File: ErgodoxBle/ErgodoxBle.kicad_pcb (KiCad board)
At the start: 2 copper layers, 179.4 x 159.7 mm, 84 parts, among them K0 KEYSW, K1 KEYSW, K10 KEYSW, K11 KEYSW, K12 KEYSW, K13 KEYSW, K14 KEYSW, K15 KEYSW, K16 KEYSW, K2 KEYSW, K20 KEYSW, K21 KEYSW, K22 KEYSW, K23 KEYSW, K24 KEYSW, K25 KEYSW, K26 KEYSW, K3 KEYSW, K30 KEYSW, K31 KEYSW, K32 KEYSW, K33 KEYSW, K34 KEYSW, K35 KEYSW, K36 KEYSW, K4 KEYSW, K40 KEYSW, K41 KEYSW, K42 KEYSW, K43 KEYSW, K44 KEYSW, K45 KEYSW, K46 KEYSW, K5 KEYSW, K54 KEYSW, K55 KEYSW, K56 KEYSW, K6 KEYSW, SW1 SW_PUSH, SW2 SW_PUSH

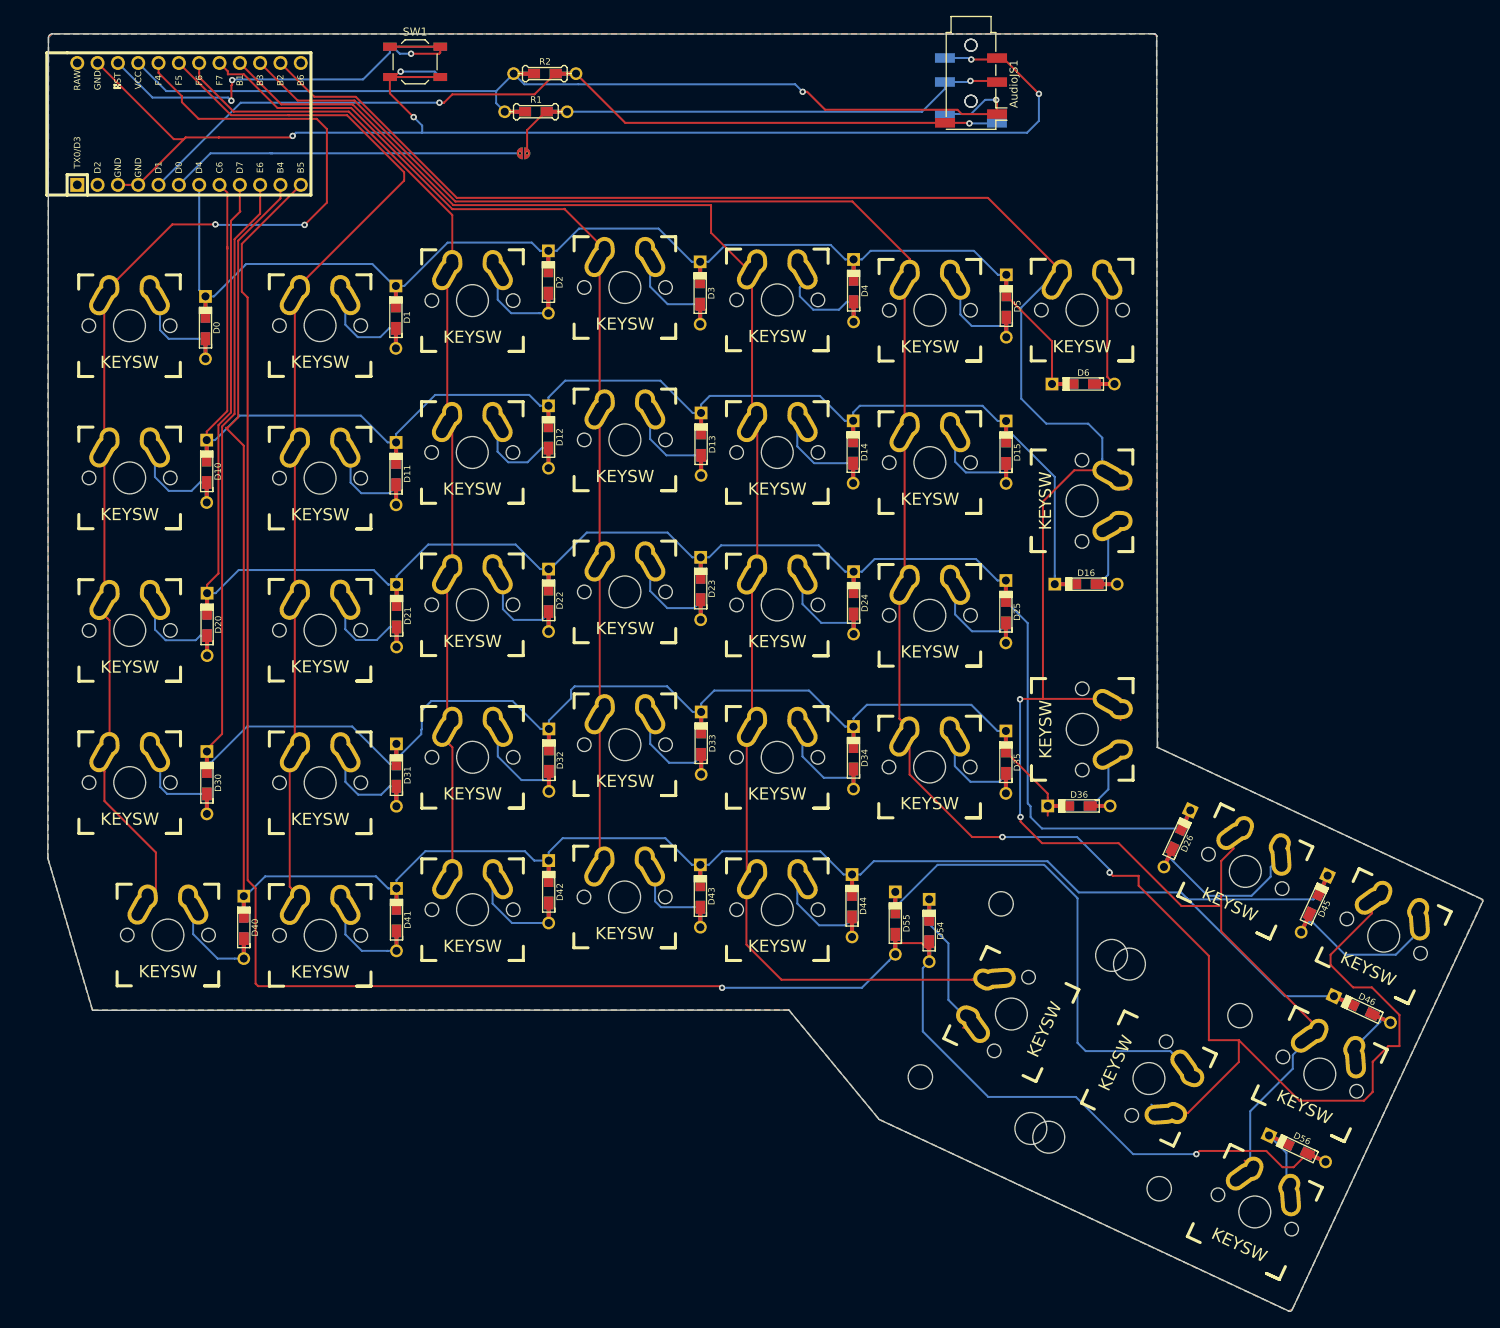
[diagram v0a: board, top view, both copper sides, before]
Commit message: align the pcb with ergodone case
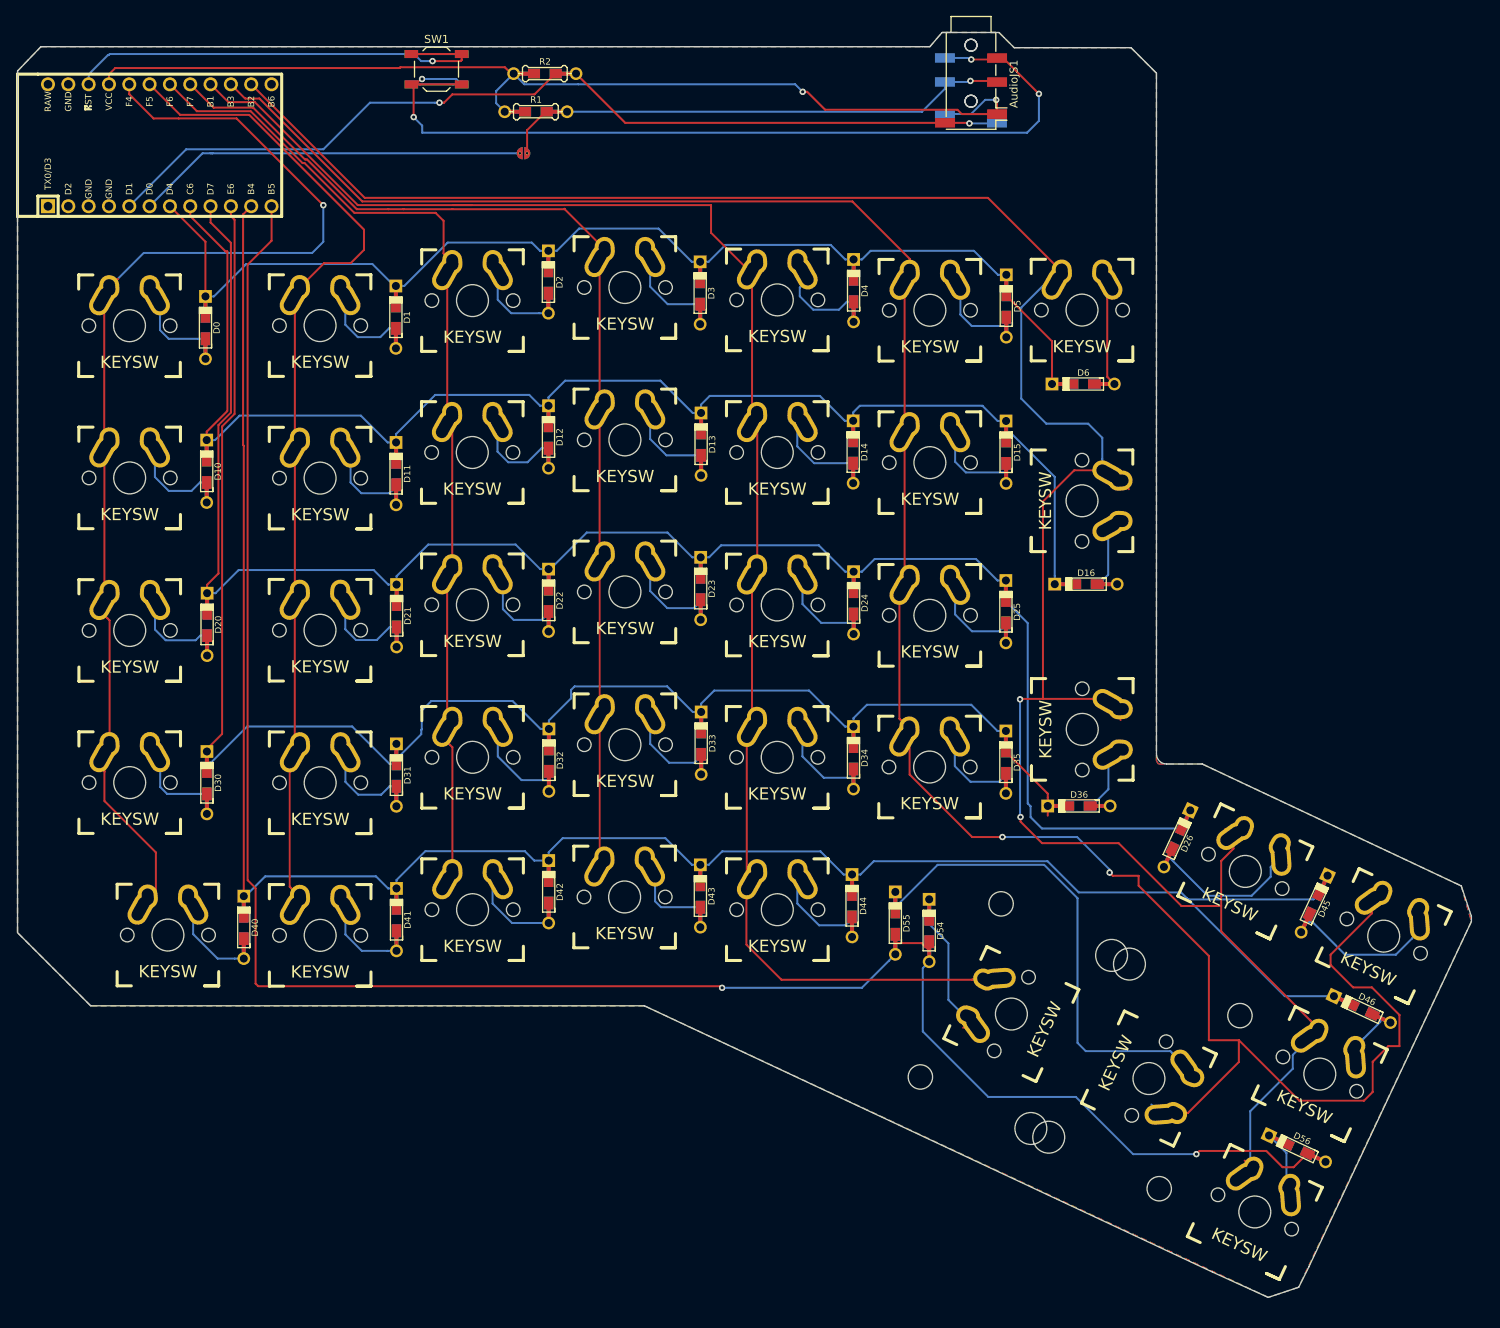
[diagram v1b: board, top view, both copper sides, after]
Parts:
- moved MCU1 4.53 mm to (36.7, 30.0)
- moved SW1 2.83 mm to (71.3, 20.5)
- moved SW2 2.83 mm to (71.3, 20.5)
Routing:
- net GND: track 178.4 -> 120.9 mm, vias 5 -> 4
- net Vcc: track 123.8 -> 131.5 mm
- net COL1: track 126.4 -> 119.8 mm
- net ROW4: track 264.7 -> 258.6 mm
- net SDAM: track 44.5 -> 49.5 mm
- net COL4: track 191.1 -> 196.0 mm
- net ROW5: track 255.3 -> 250.6 mm
- net scl: track 111.8 -> 116.5 mm
- net ROW3: track 207.4 -> 203.6 mm
- net COL6: track 293.0 -> 295.5 mm
- net COL5: track 281.2 -> 283.8 mm
- net ROW2: track 219.5 -> 217.4 mm
- net COL3: track 129.6 -> 131.6 mm
- net RST: track 60.7 -> 62.7 mm, vias 3 -> 1
- net ROW1: track 170.2 -> 168.9 mm
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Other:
- board size 179.4 x 159.7 mm -> 181.7 x 158.1 mm

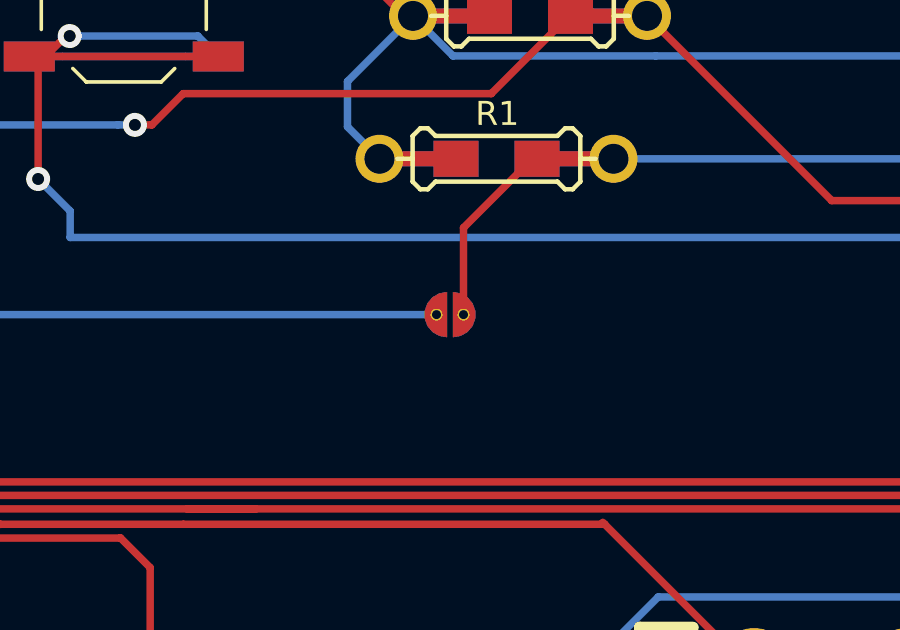
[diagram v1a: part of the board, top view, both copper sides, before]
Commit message: add solder jumpber on both layers
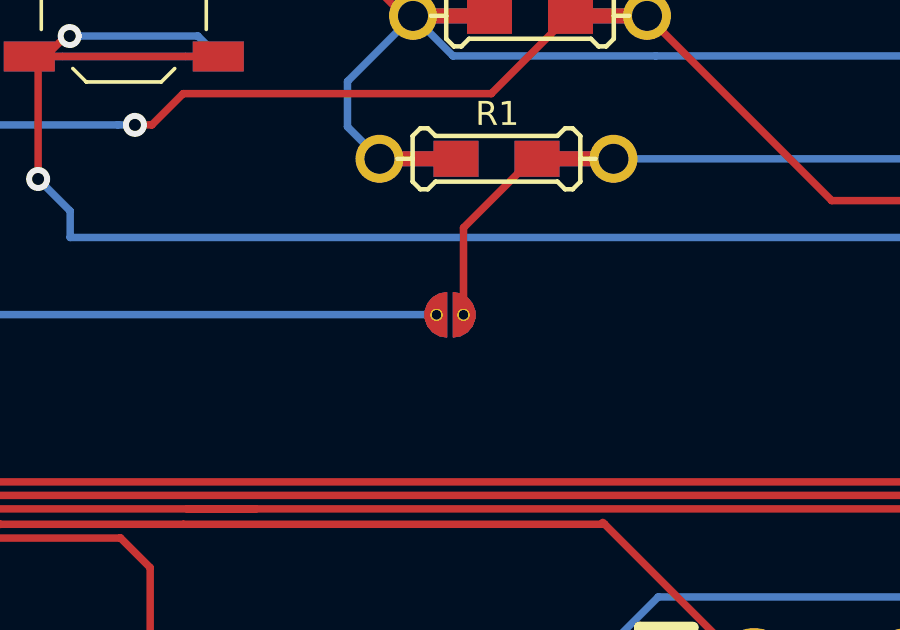
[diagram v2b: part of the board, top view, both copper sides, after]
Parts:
- added SJ2: SOLDER_JUMPER, Keebio-Parts:solder_jumper, B.Cu at (82.2, 31.0)
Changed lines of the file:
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@@
     (tracks 685)
     (zones 0)
-    (modules 84)
+    (modules 85)
     (nets 62)
   )
@@
     )
   )
+  (module Keebio-Parts:solder_jumper (layer B.Cu)
+    (at 82.169 30.988)
+    (solder_mask_margin 0.001)
+    (solder_paste_margin -0.02)
+    (clearance 0.001)
+    (fp_text reference SJ2 (at -0.508 -1.016) (layer Cmts.User) hide
+      (effects (font (size 0.3 0.3) (thickness 0.03)))
+    )
+    (fp_text value SOLDER_JUMPER (at 0 1.524) (layer B.SilkS) hide
+      (effects (font (size 0.4 0.4) (thickness 0.04)) (justify mirror))
+    )
+    (fp_poly (pts (xy -0.1 0.75) (xy -0.3565 0.7048) (xy -0.5821 0.5745) (xy -0.7495 0.375)
+      (xy -0.8386 0.1302) (xy -0.8386 -0.1302) (xy -0.7495 -0.375) (xy -0.5821 -0.5745)
+      (xy -0.3565 -0.7048) (xy -0.1 -0.75) (xy -0.1 0.75)) (layer B.Cu) (width 0.01))
+    (fp_poly (pts (xy 0.1 -0.75) (xy 0.3565 -0.7048) (xy 0.5821 -0.5745) (xy 0.7495 -0.375)
+      (xy 0.8386 -0.1302) (xy 0.8386 0.1302) (xy 0.7495 0.375) (xy 0.5821 0.5745)
+      (xy 0.3565 0.7048) (xy 0.1 0.75) (xy 0.1 -0.75)) (layer B.Cu) (width 0.01))
+    (fp_poly (pts (xy -0.1 0.75) (xy -0.3565 0.7048) (xy -0.5821 0.5745) (xy -0.7495 0.375)
+      (xy -0.8386 0.1302) (xy -0.8386 -0.1302) (xy -0.7495 -0.375) (xy -0.5821 -0.5745)
+      (xy -0.3565 -0.7048) (xy -0.1 -0.75) (xy -0.1 0.75)) (layer F.Cu) (width 0.01))
+    (fp_poly (pts (xy 0.1 -0.75) (xy 0.3565 -0.7048) (xy 0.5821 -0.5745) (xy 0.7495 -0.375)
+      (xy 0.8386 -0.1302) (xy 0.8386 0.1302) (xy 0.7495 0.375) (xy 0.5821 0.5745)
+      (xy 0.3565 0.7048) (xy 0.1 0.75) (xy 0.1 -0.75)) (layer F.Cu) (width 0.01))
+    (pad 1 thru_hole circle (at -0.45 0) (size 0.4 0.4) (drill 0.3) (layers *.Cu *.Mask)
+      (net 57 SDAM))
+    (pad 2 thru_hole circle (at 0.45 0) (size 0.4 0.4) (drill 0.3) (layers *.Cu *.Mask)
+      (net 58 sda))
+  )
   (gr_line (start 132.08 17.653) (end 132.969 17.653) (layer Edge.Cuts) (width 0.15))

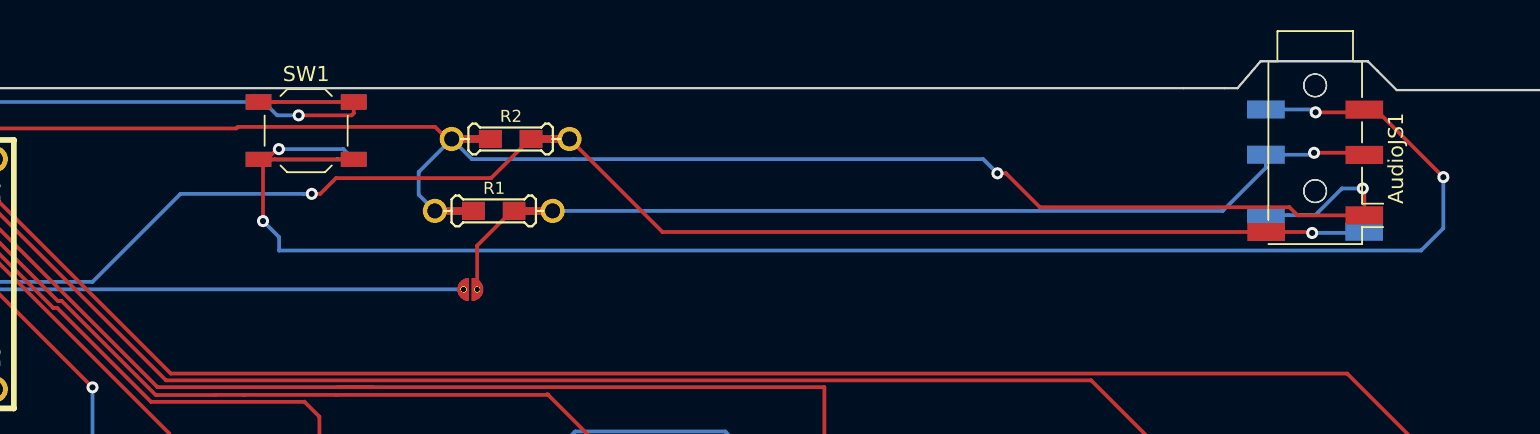
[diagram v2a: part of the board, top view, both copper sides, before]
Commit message: added clearence for ProtonC
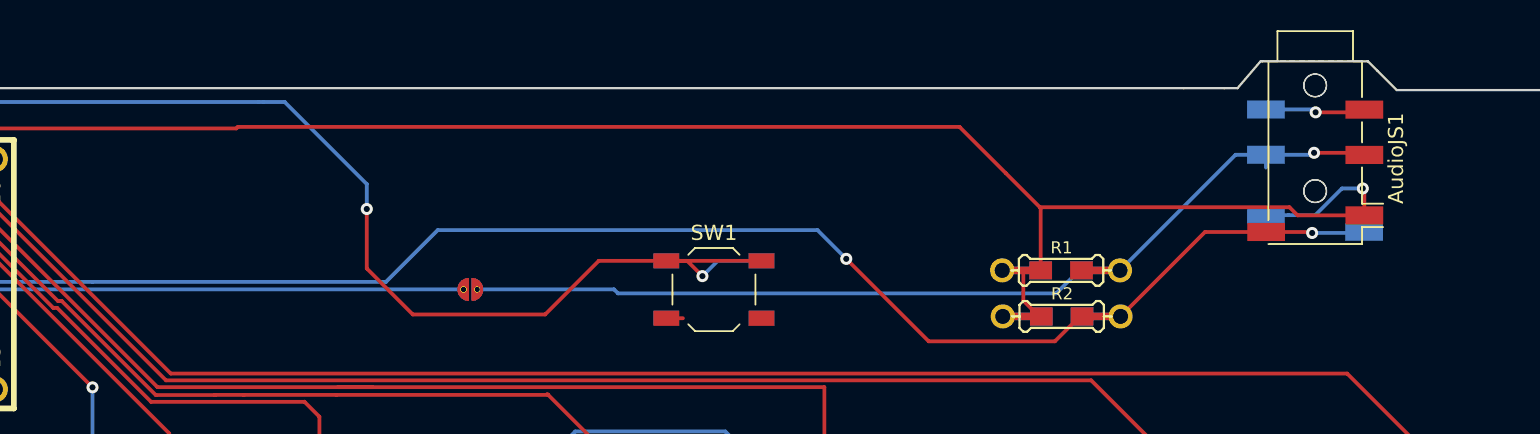
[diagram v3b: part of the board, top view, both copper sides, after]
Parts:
- moved R2 38.3 mm to (121.3, 32.8)
- moved R1 37.8 mm to (121.3, 29.7)
- moved SW1 29.0 mm to (98.3, 31.0)
- moved SW2 29.0 mm to (98.3, 31.0)
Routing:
- net GND: track 120.9 -> 8.53 mm, vias 4 -> 1
- net RST: track 62.7 -> 93.6 mm, vias 1 -> 2
- net sda: track 62.2 -> 61.1 mm
- net Vcc: track 131.5 -> 131.8 mm, vias 2 -> 1
